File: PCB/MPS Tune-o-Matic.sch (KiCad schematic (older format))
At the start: 16 parts, among them J1 ISP, J2 MPS, U1 ATmega328P, Y1 FA-238 16.0000MB-C3

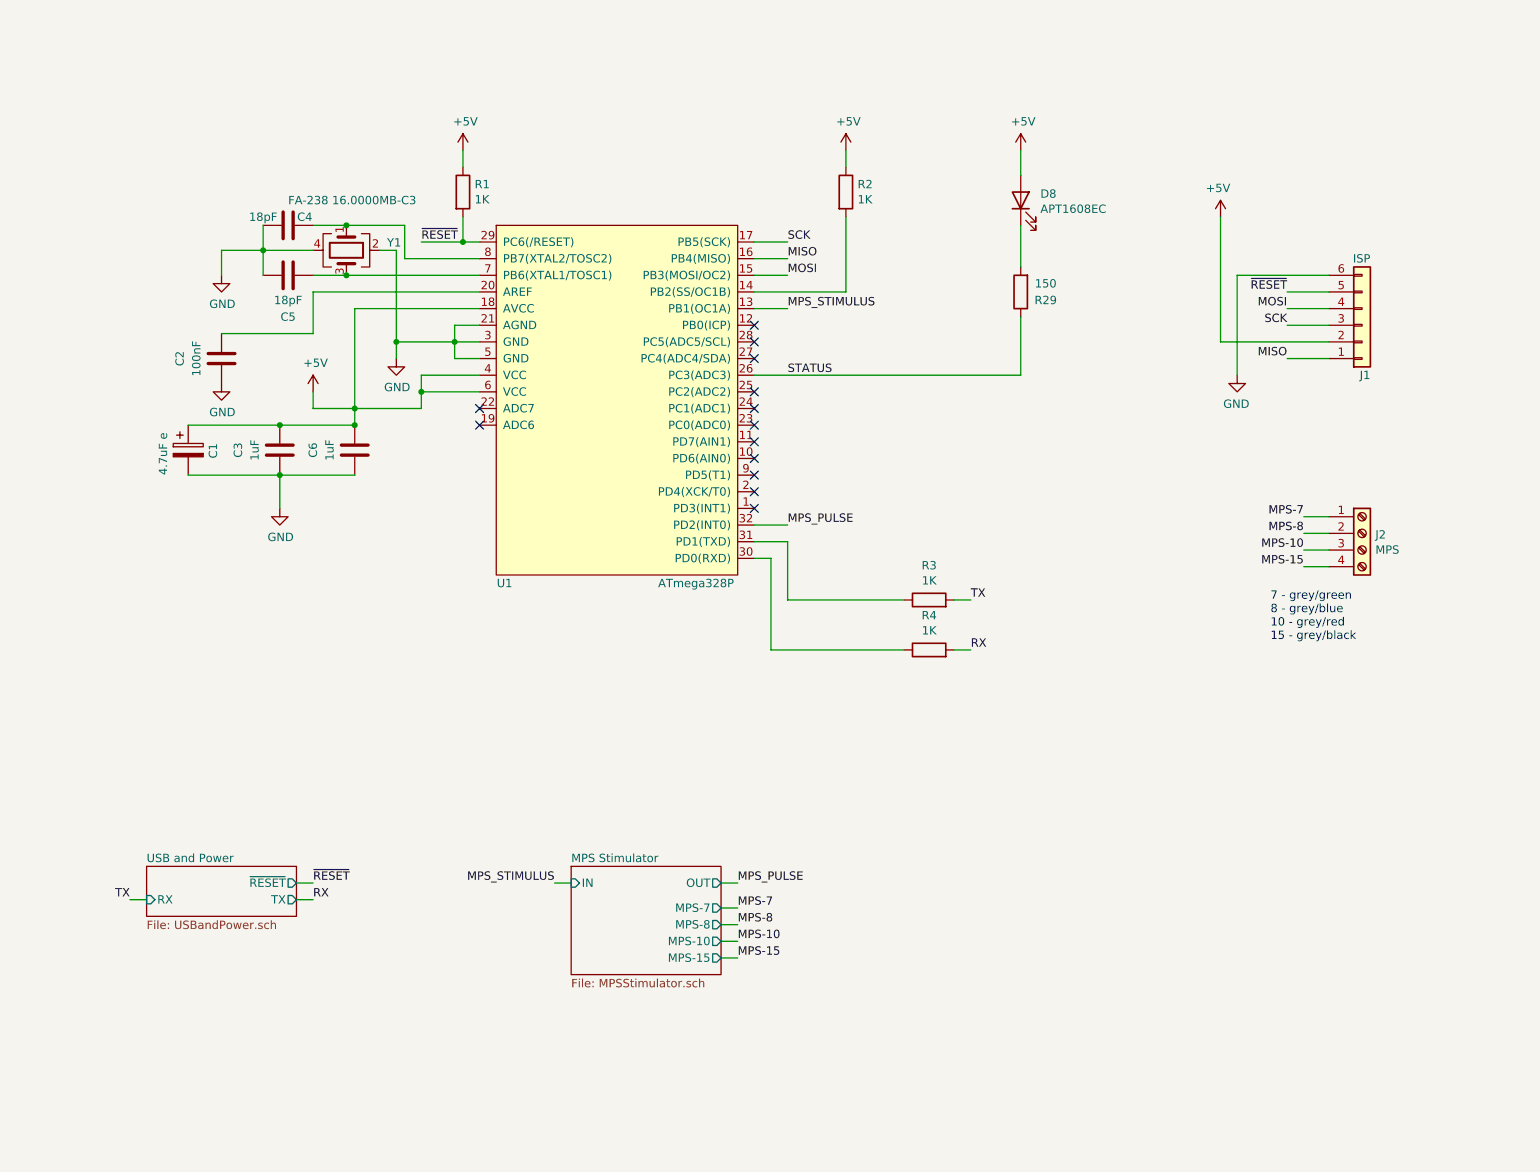
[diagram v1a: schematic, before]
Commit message: Added pressure sensor.
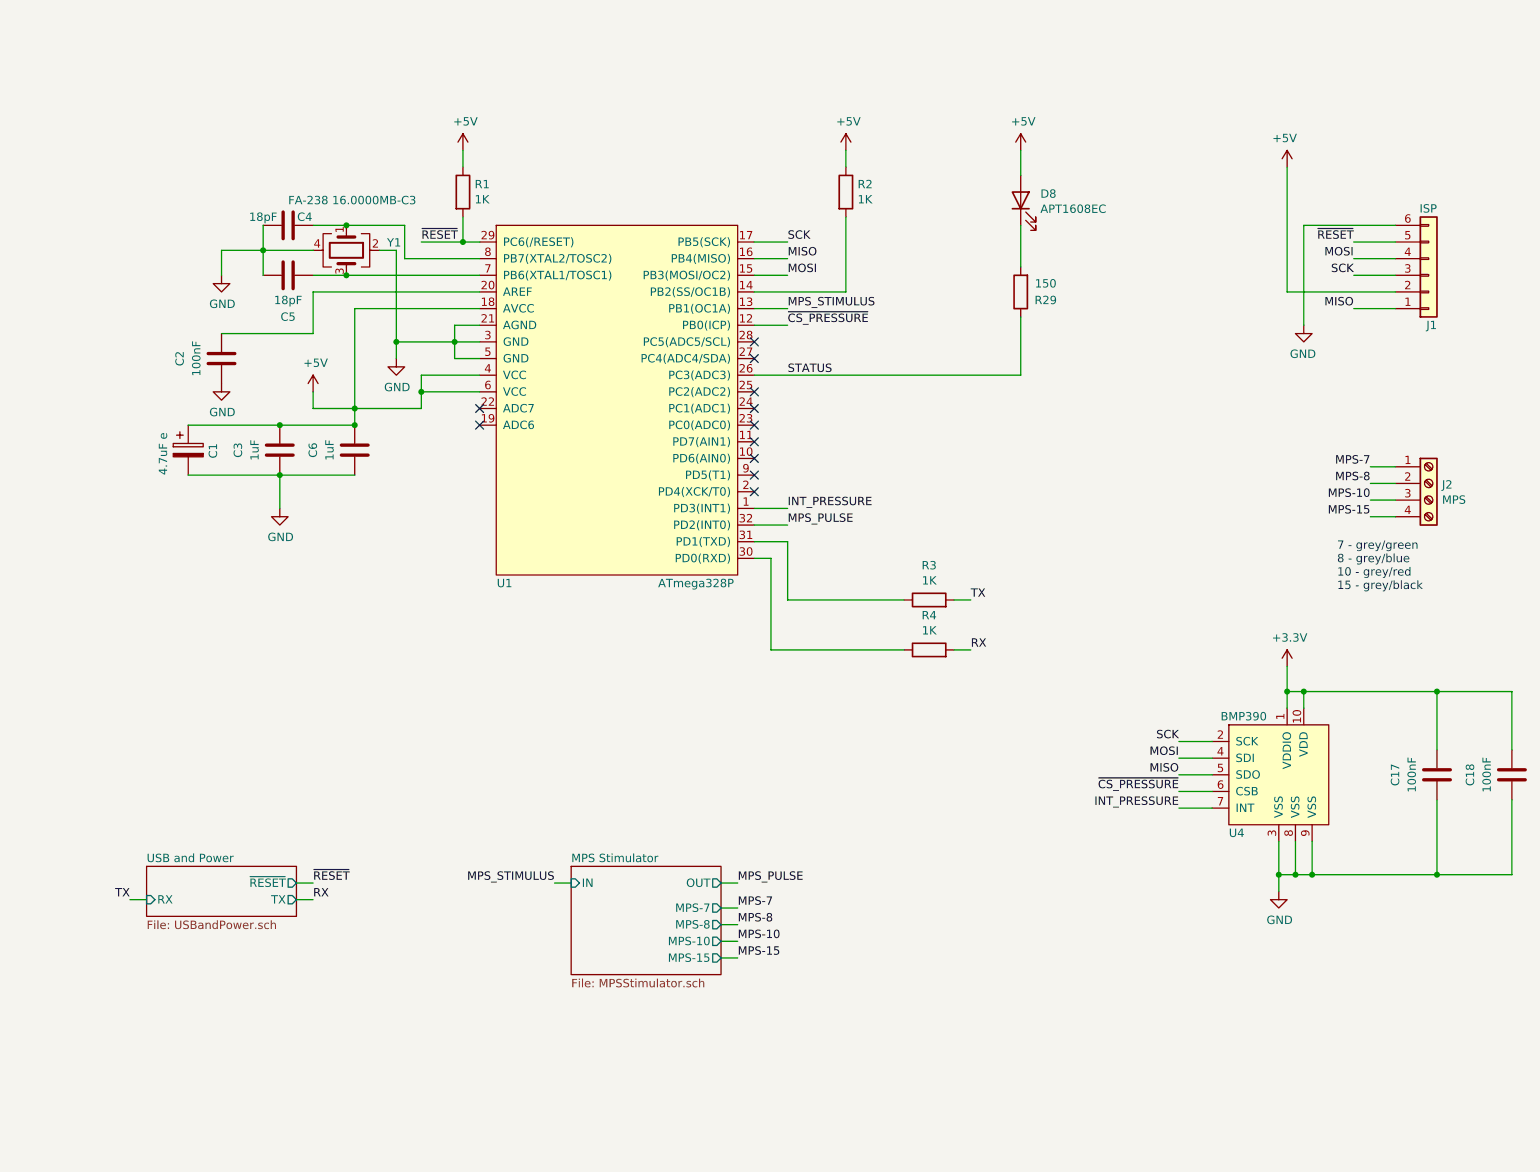
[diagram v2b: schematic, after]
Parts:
- added C17, C18: 100nF, Capacitor_SMD:C_0603_1608Metric, symbol Device:C
- added U4: BMP390, Britishideas:LGA-2x2-10-pin, symbol BritishIdeas:BMP390
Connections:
- net GND: now also C17.2, C18.2, U4.3 (VSS), U4.8 (VSS), U4.9 (VSS)
- net MISO: now also U4.5 (SDO)
- net MOSI: now also U4.4 (SDI)
- net SCK: now also U4.2 (SCK)
- net INT_PRESSURE: now reaches U1.1 (PD3(INT1))
- net INT_PRESSURE: now also U4.7 (INT)
- net ~CS_PRESSURE: now reaches U1.12 (PB0(ICP))
- net ~CS_PRESSURE: now also U4.6 (CSB)
- new net +3V3: C17.1, C18.1, U4.1 (VDDIO), U4.10 (VDD)
- no-connect marks 13 -> 11
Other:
- moved on the sheet: J1, J2
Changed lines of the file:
@@
 L Connector_Generic:Conn_01x06 J1
 U 1 1 5FE92E63
-P 8900 2600
-F 0 "J1" H 8950 2900 50  0000 R CNN
-F 1 "ISP" H 8950 2200 50  0000 R CNN
-F 2 "Connector_PinHeader_2.54mm:PinHeader_2x03_P2.54mm_Vertical" H 8900 2600 50  0001 C CNN
-F 3 "~" H 8900 2600 50  0001 C CNN
-	1    8900 2600
+P 9300 2300
+F 0 "J1" H 9350 2600 50  0000 R CNN
+F 1 "ISP" H 9350 1900 50  0000 R CNN
+F 2 "Connector_PinHeader_2.54mm:PinHeader_2x03_P2.54mm_Vertical" H 9300 2300 50  0001 C CNN
+F 3 "~" H 9300 2300 50  0001 C CNN
+	1    9300 2300
 	1    0    0    1
 $EndComp
 Wire Wire Line
-	8700 2400 8450 2400
-Wire Wire Line
-	8700 2500 8450 2500
-Wire Wire Line
-	8700 2600 8450 2600
-Wire Wire Line
-	8700 2800 8450 2800
-Text Label 8450 2800 2    50   ~ 0
+	9100 2100 8850 2100
+Wire Wire Line
+	9100 2200 8850 2200
+Wire Wire Line
+	9100 2300 8850 2300
+Wire Wire Line
+	9100 2500 8850 2500
+Text Label 8850 2500 2    50   ~ 0
 MISO
 Wire Wire Line
@@
 MISO
 Wire Wire Line
-	8050 2700 8050 1950
-Wire Wire Line
-	8700 2700 8050 2700
+	8450 2400 8450 1650
+Wire Wire Line
+	9100 2400 8450 2400
 $Comp
 L power:+5V #PWR08
 U 1 1 5FE94D36
-P 8050 1950
-F 0 "#PWR08" H 8050 1800 50  0001 C CNN
-F 1 "+5V" H 8065 2123 50  0000 C CNN
-F 2 "" H 8050 1950 50  0001 C CNN
-F 3 "" H 8050 1950 50  0001 C CNN
-	1    8050 1950
+P 8450 1650
+F 0 "#PWR08" H 8450 1500 50  0001 C CNN
+F 1 "+5V" H 8465 1823 50  0000 C CNN
+F 2 "" H 8450 1650 50  0001 C CNN
+F 3 "" H 8450 1650 50  0001 C CNN
+	1    8450 1650
 	-1   0    0    -1
 $EndComp
-Text Label 8450 2600 2    50   ~ 0
+Text Label 8850 2300 2    50   ~ 0
 SCK
 Wire Wire Line
@@
 Text Label 5450 2100 0    50   ~ 0
 SCK
-Text Label 8450 2500 2    50   ~ 0
+Text Label 8850 2200 2    50   ~ 0
 MOSI
 Wire Wire Line
@@
 Text Label 5450 2300 0    50   ~ 0
 MOSI
-Text Label 8450 2400 2    50   ~ 0
+Text Label 8850 2100 2    50   ~ 0
 ~RESET
 Wire Wire Line
@@
 ~RESET
 Wire Wire Line
-	8150 2300 8150 2900
-Wire Wire Line
-	8700 2300 8150 2300
+	8550 2000 8550 2600
+Wire Wire Line
+	9100 2000 8550 2000
 $Comp
 L power:GND #PWR09
 U 1 1 5FE95B1A
-P 8150 2900
-F 0 "#PWR09" H 8150 2650 50  0001 C CNN
-F 1 "GND" H 8155 2727 50  0000 C CNN
-F 2 "" H 8150 2900 50  0001 C CNN
-F 3 "" H 8150 2900 50  0001 C CNN
-	1    8150 2900
+P 8550 2600
+F 0 "#PWR09" H 8550 2350 50  0001 C CNN
+F 1 "GND" H 8555 2427 50  0000 C CNN
+F 2 "" H 8550 2600 50  0001 C CNN
+F 3 "" H 8550 2600 50  0001 C CNN
+	1    8550 2600
 	-1   0    0    -1
 $EndComp
@@
 Wire Wire Line
 	2500 6050 2600 6050
-Text Label 8550 3750 2    50   ~ 0
+Text Label 8950 3450 2    50   ~ 0
 MPS-7
-Text Label 8550 4050 2    50   ~ 0
+Text Label 8950 3750 2    50   ~ 0
 MPS-15
-Text Label 8550 3950 2    50   ~ 0
+Text Label 8950 3650 2    50   ~ 0
 MPS-10
-Text Label 8550 3850 2    50   ~ 0
+Text Label 8950 3550 2    50   ~ 0
 MPS-8
-Text Notes 8350 4500 0    50   ~ 0
+Text Notes 8750 4200 0    50   ~ 0
 7 - grey/green\n8 - grey/blue\n10 - grey/red\n15 - grey/black
 $Comp
@@
 NoConn ~ 5250 3500
 NoConn ~ 5250 3600
-NoConn ~ 5250 3700
 $Comp
 L Connector:Screw_Terminal_01x04 J2
 U 1 1 635F711E
-P 8900 3850
-F 0 "J2" H 8980 3842 50  0000 L CNN
-F 1 "MPS" H 8980 3751 50  0000 L CNN
-F 2 "Britishideas:PhoenixContact_COMBICON_PT_4" H 8900 3850 50  0001 C CNN
-F 3 "~" H 8900 3850 50  0001 C CNN
-F 4 "1935792" H 8900 3850 50  0001 C CNN "manf#"
-F 5 "1935187" H 8900 3850 50  0001 C CNN "manf2#"
-	1    8900 3850
-	1    0    0    -1
-$EndComp
-Wire Wire Line
-	8550 4050 8700 4050
-Wire Wire Line
-	8700 3950 8550 3950
-Wire Wire Line
-	8550 3850 8700 3850
-Wire Wire Line
-	8700 3750 8550 3750
+P 9300 3550
+F 0 "J2" H 9380 3542 50  0000 L CNN
+F 1 "MPS" H 9380 3451 50  0000 L CNN
+F 2 "Britishideas:PhoenixContact_COMBICON_PT_4" H 9300 3550 50  0001 C CNN
+F 3 "~" H 9300 3550 50  0001 C CNN
+F 4 "1935792" H 9300 3550 50  0001 C CNN "manf#"
+F 5 "1935187" H 9300 3550 50  0001 C CNN "manf2#"
+	1    9300 3550
+	1    0    0    -1
+$EndComp
+Wire Wire Line
+	8950 3750 9100 3750
+Wire Wire Line
+	9100 3650 8950 3650
+Wire Wire Line
+	8950 3550 9100 3550
+Wire Wire Line
+	9100 3450 8950 3450
 $Comp
 L Device:LED D8
@@
 Wire Wire Line
 	6850 2550 6850 2900
-NoConn ~ 5250 2600
 NoConn ~ 5250 2700
 NoConn ~ 5250 3100
@@
 Text Label 5450 2900 0    50   ~ 0
 STATUS
+$Comp
+L BritishIdeas:BMP390 U4
+U 1 1 63612A1B
+P 8100 5600
+F 0 "U4" H 8100 5550 50  0000 L CNN
+F 1 "BMP390" H 8050 6250 50  0000 L CNN
+F 2 "Britishideas:LGA-2x2-10-pin" H 8100 5600 50  0001 C CNN
+F 3 "" H 8100 5600 50  0001 C CNN
+F 4 "BMP390" H 8100 5600 50  0001 C CNN "manf#"
+	1    8100 5600
+	1    0    0    -1
+$EndComp
+Text Label 7800 5100 2    50   ~ 0
+SCK
+Text Label 7800 5300 2    50   ~ 0
+MISO
+Text Label 7800 5200 2    50   ~ 0
+MOSI
+Text Label 7800 5400 2    50   ~ 0
+~CS_PRESSURE
+Text Label 7800 5500 2    50   ~ 0
+INT_PRESSURE
+Wire Wire Line
+	7800 5500 8000 5500
+Wire Wire Line
+	8000 5400 7800 5400
+Wire Wire Line
+	7800 5300 8000 5300
+Wire Wire Line
+	8000 5200 7800 5200
+Wire Wire Line
+	7800 5100 8000 5100
+Text Label 5450 2600 0    50   ~ 0
+~CS_PRESSURE
+Wire Wire Line
+	5450 2600 5250 2600
+Text Label 5450 3700 0    50   ~ 0
+INT_PRESSURE
+Wire Wire Line
+	5450 3700 5250 3700
+$Comp
+L power:GND #PWR036
+U 1 1 63625441
+P 8400 6000
+F 0 "#PWR036" H 8400 5750 50  0001 C CNN
+F 1 "GND" H 8405 5827 50  0000 C CNN
+F 2 "" H 8400 6000 50  0001 C CNN
+F 3 "" H 8400 6000 50  0001 C CNN
+	1    8400 6000
+	1    0    0    -1
+$EndComp
+Wire Wire Line
+	8400 6000 8400 5900
+Wire Wire Line
+	8600 5700 8600 5900
+Wire Wire Line
+	8600 5900 8500 5900
+Connection ~ 8400 5900
+Wire Wire Line
+	8400 5900 8400 5700
+Wire Wire Line
+	8500 5700 8500 5900
+Connection ~ 8500 5900
+Wire Wire Line
+	8500 5900 8400 5900
+$Comp
+L Device:C C17
+U 1 1 6362E39E
+P 9350 5300
+F 0 "C17" V 9600 5300 50  0000 C CNN
+F 1 "100nF" V 9500 5300 50  0000 C CNN
+F 2 "Capacitor_SMD:C_0603_1608Metric" H 9388 5150 50  0001 C CNN
+F 3 "~" H 9350 5300 50  0001 C CNN
+	1    9350 5300
+	-1   0    0    -1
+$EndComp
+$Comp
+L Device:C C18
+U 1 1 6362EBD1
+P 9800 5300
+F 0 "C18" V 10050 5300 50  0000 C CNN
+F 1 "100nF" V 9950 5300 50  0000 C CNN
+F 2 "Capacitor_SMD:C_0603_1608Metric" H 9838 5150 50  0001 C CNN
+F 3 "~" H 9800 5300 50  0001 C CNN
+	1    9800 5300
+	-1   0    0    -1
+$EndComp
+Wire Wire Line
+	9800 5450 9800 5900
+Wire Wire Line
+	9800 5900 9350 5900
+Connection ~ 8600 5900
+Wire Wire Line
+	9350 5450 9350 5900
+Connection ~ 9350 5900
+Wire Wire Line
+	9350 5900 8600 5900
+Wire Wire Line
+	8550 4900 8550 4800
+Wire Wire Line
+	8550 4800 9350 4800
+Wire Wire Line
+	9350 4800 9350 5150
+Wire Wire Line
+	9800 5150 9800 4800
+Wire Wire Line
+	9800 4800 9350 4800
+Connection ~ 9350 4800
+Wire Wire Line
+	8450 4900 8450 4800
+Wire Wire Line
+	8450 4800 8550 4800
+Connection ~ 8550 4800
+$Comp
+L power:+3.3V #PWR037
+U 1 1 6363EC4A
+P 8450 4650
+F 0 "#PWR037" H 8450 4500 50  0001 C CNN
+F 1 "+3.3V" H 8465 4823 50  0000 C CNN
+F 2 "" H 8450 4650 50  0001 C CNN
+F 3 "" H 8450 4650 50  0001 C CNN
+	1    8450 4650
+	1    0    0    -1
+$EndComp
+Wire Wire Line
+	8450 4650 8450 4800
+Connection ~ 8450 4800
 $EndSCHEMATC

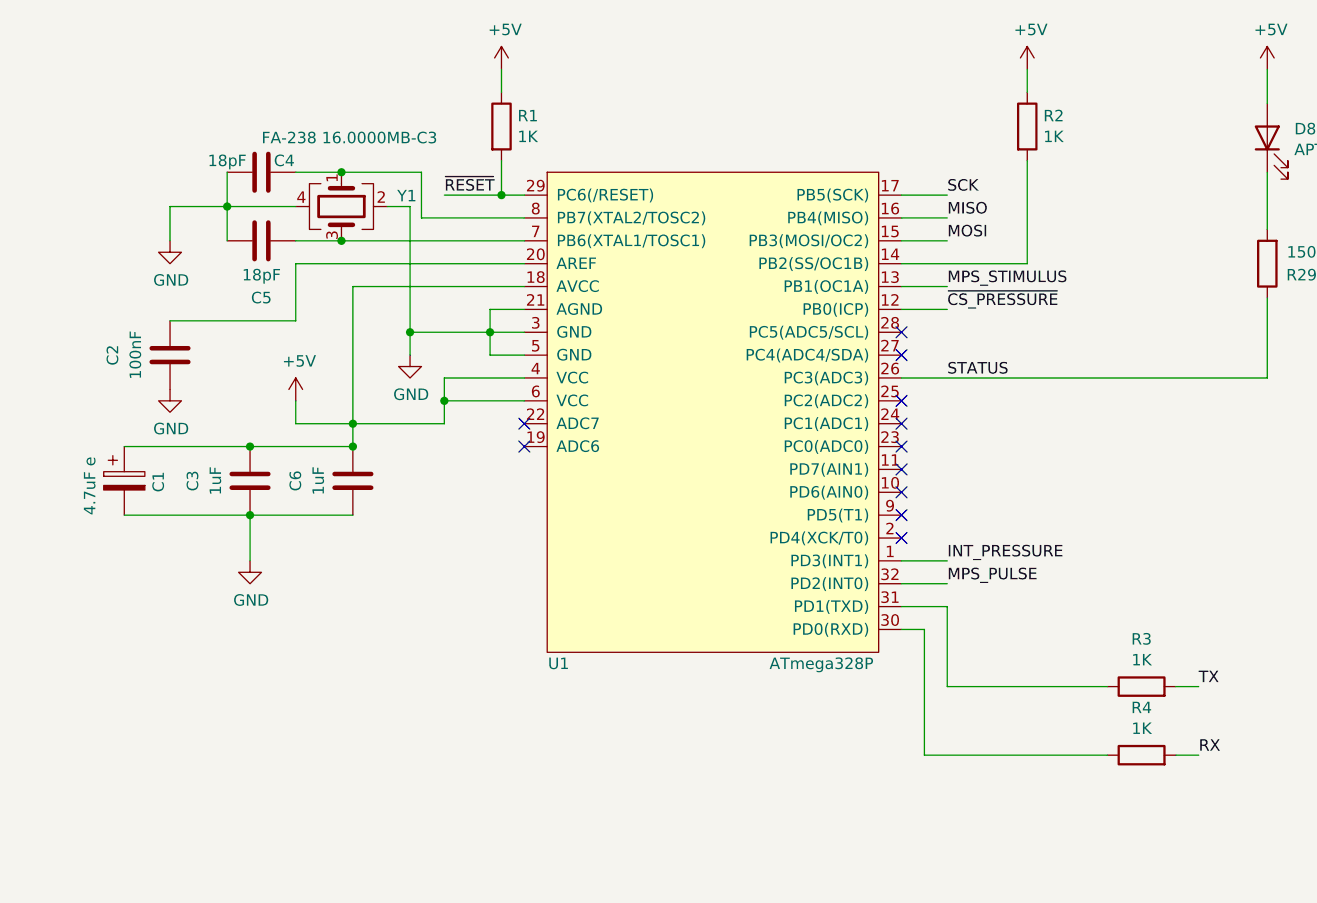
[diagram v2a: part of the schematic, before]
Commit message: Added LED for 12V power. Added resistor on MPS_STIMULUS signal. Moved track away from mounting hole. Fixed orientation of diodes. Added PDF of schematic. Updated manufacturing files.
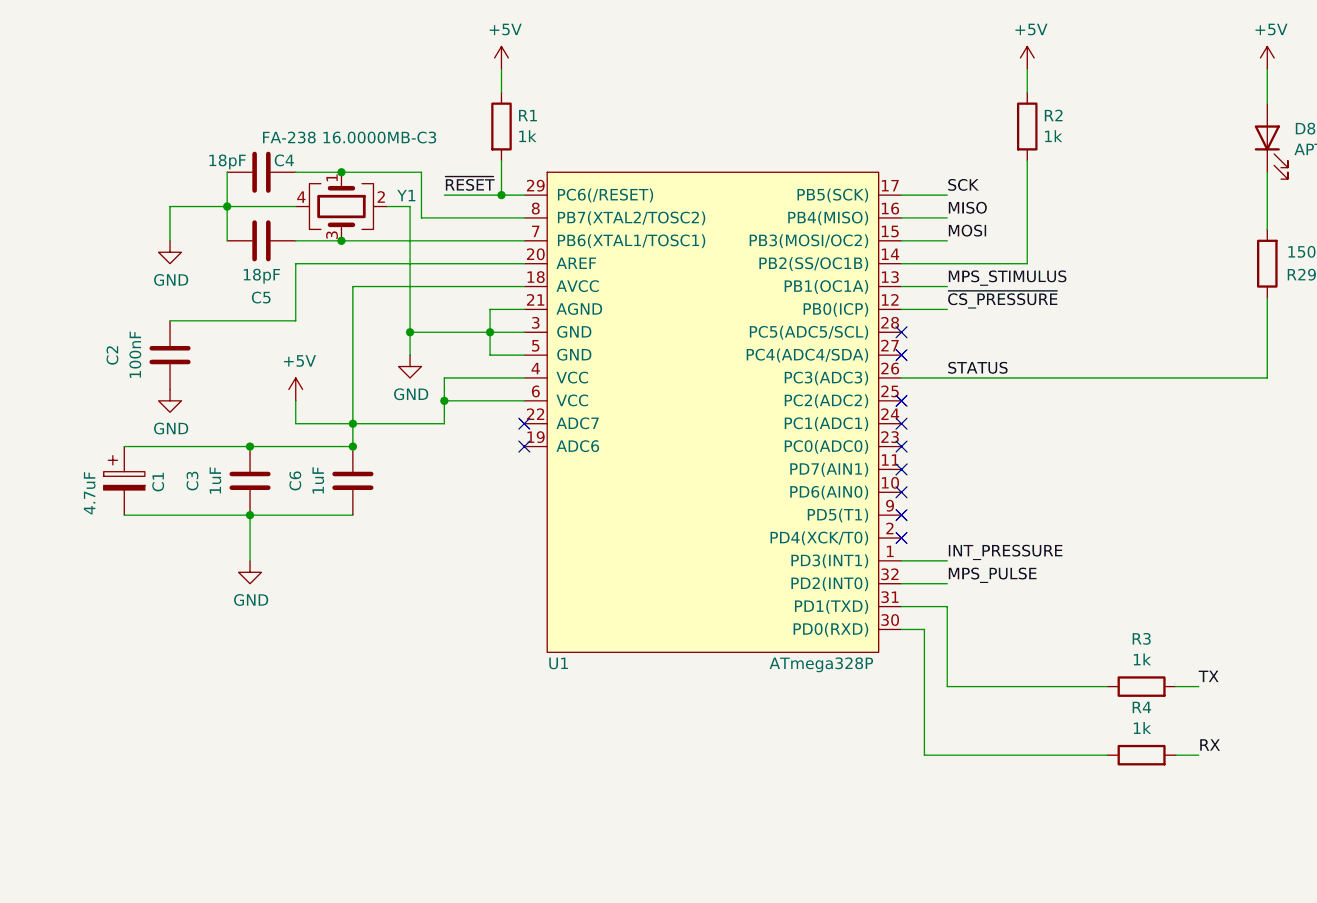
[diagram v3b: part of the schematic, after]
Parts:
- C1: value 4.7uF e -> 4.7uF
- R1, R2, R3, R4: value 1K -> 1k
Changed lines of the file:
@@
 Sheet 1 3
 Title "MPS Tune-o-Matic"
-Date "2022-10-31"
-Rev "V1.0"
+Date "2022-11-10"
+Rev "V1.1"
 Comp "(C) andy@britishideas.com 2022"
 Comment1 "For Bosch D-Jetronic MPS Type 3"
@@
 P 3500 1800
 F 0 "R1" H 3570 1846 50  0000 L CNN
-F 1 "1K" H 3570 1755 50  0000 L CNN
+F 1 "1k" H 3570 1755 50  0000 L CNN
 F 2 "Resistor_SMD:R_0603_1608Metric" V 3430 1800 50  0001 C CNN
 F 3 "~" H 3500 1800 50  0001 C CNN
@@
 P 1850 3350
 F 0 "C1" V 2000 3300 50  0000 L CNN
-F 1 "4.7uF e" V 1700 3200 50  0000 L CNN
+F 1 "4.7uF" V 1700 3200 50  0000 L CNN
 F 2 "Capacitor_SMD:C_0603_1608Metric" H 1888 3200 50  0001 C CNN
 F 3 "~" H 1850 3350 50  0001 C CNN
@@
 P 6300 4250
 F 0 "R3" V 6507 4250 50  0000 C CNN
-F 1 "1K" V 6416 4250 50  0000 C CNN
+F 1 "1k" V 6416 4250 50  0000 C CNN
 F 2 "Resistor_SMD:R_0603_1608Metric" V 6230 4250 50  0001 C CNN
 F 3 "~" H 6300 4250 50  0001 C CNN
@@
 P 6300 4550
 F 0 "R4" V 6507 4550 50  0000 C CNN
-F 1 "1K" V 6416 4550 50  0000 C CNN
+F 1 "1k" V 6416 4550 50  0000 C CNN
 F 2 "Resistor_SMD:R_0603_1608Metric" V 6230 4550 50  0001 C CNN
 F 3 "~" H 6300 4550 50  0001 C CNN
@@
 P 5800 1800
 F 0 "R2" H 5870 1846 50  0000 L CNN
-F 1 "1K" H 5870 1755 50  0000 L CNN
+F 1 "1k" H 5870 1755 50  0000 L CNN
 F 2 "Resistor_SMD:R_0603_1608Metric" V 5730 1800 50  0001 C CNN
 F 3 "~" H 5800 1800 50  0001 C CNN
